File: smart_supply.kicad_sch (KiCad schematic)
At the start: 0 parts

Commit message: unify files
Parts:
- added C2: 0.1u, symbol Device:C
- added I1: ISIN, Package_SO:SOIC-20W_7.5x12.8mm_P1.27mm, symbol Simulation_SPICE:ISIN
- added R1: 50, symbol Device:R
- added R3, R4, R7, R8: 10k, symbol Device:R
- added R5: 220, symbol Device:R
- added R6: 10, symbol Device:R
- added TR1: ZMCT103C, Transformer_THT:Transformer_Zeming_ZMCT103C, symbol Transformer:ZMCT103C
- added V1: 3.3, symbol Simulation_SPICE:VDC
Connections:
- new net: I1.1, R5.1, R6.1
- new net: I1.2, R5.2, R7.1, R8.2
- new net: R8.1, V1.1
- new net: C2.2, R6.2
- new net: R1.2, R3.1, R4.2, TR1.2
- new net +3.3V: R3.2
- new net 0: C2.1, R7.2, V1.2
- new net GND: R4.1
- new net c_sns: R1.1, TR1.1
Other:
- note added: ".tran 0 200m 50m 10u"

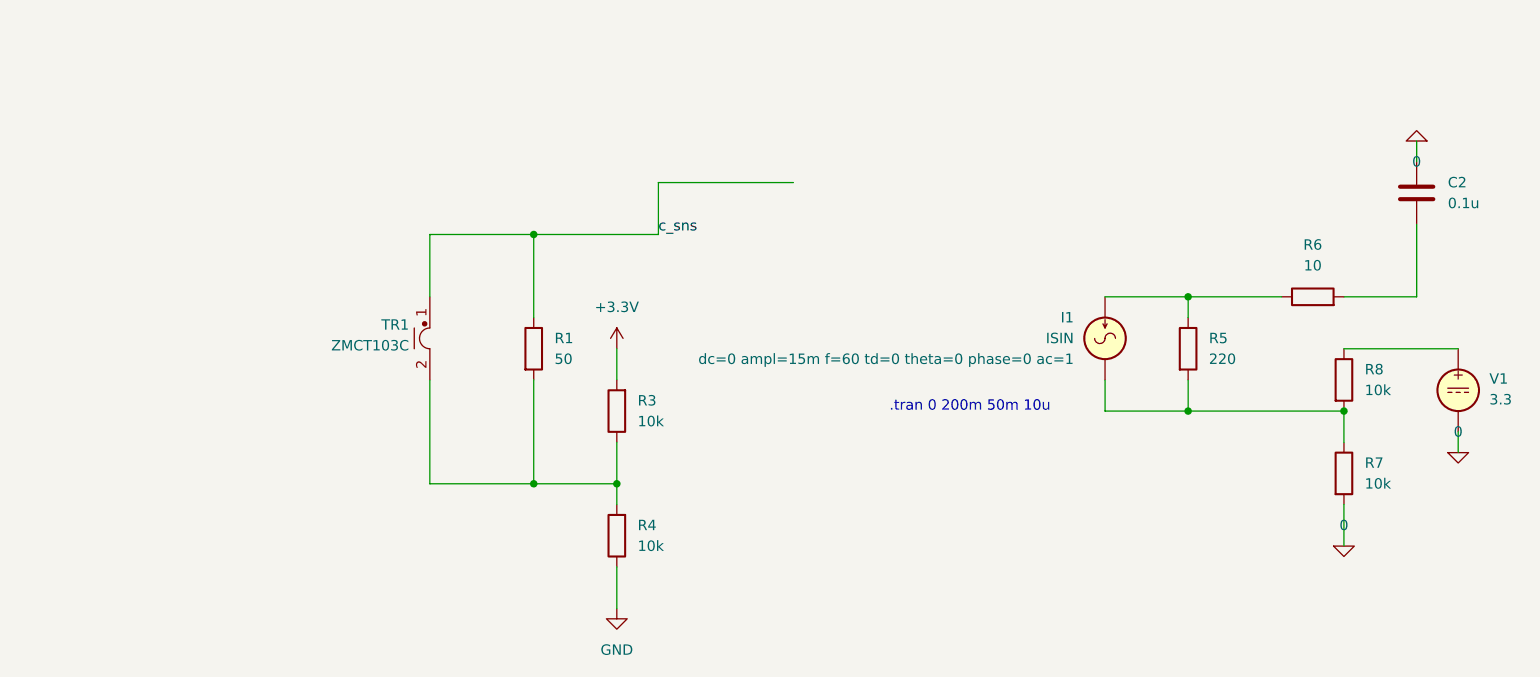
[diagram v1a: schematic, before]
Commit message: add current sense simulation
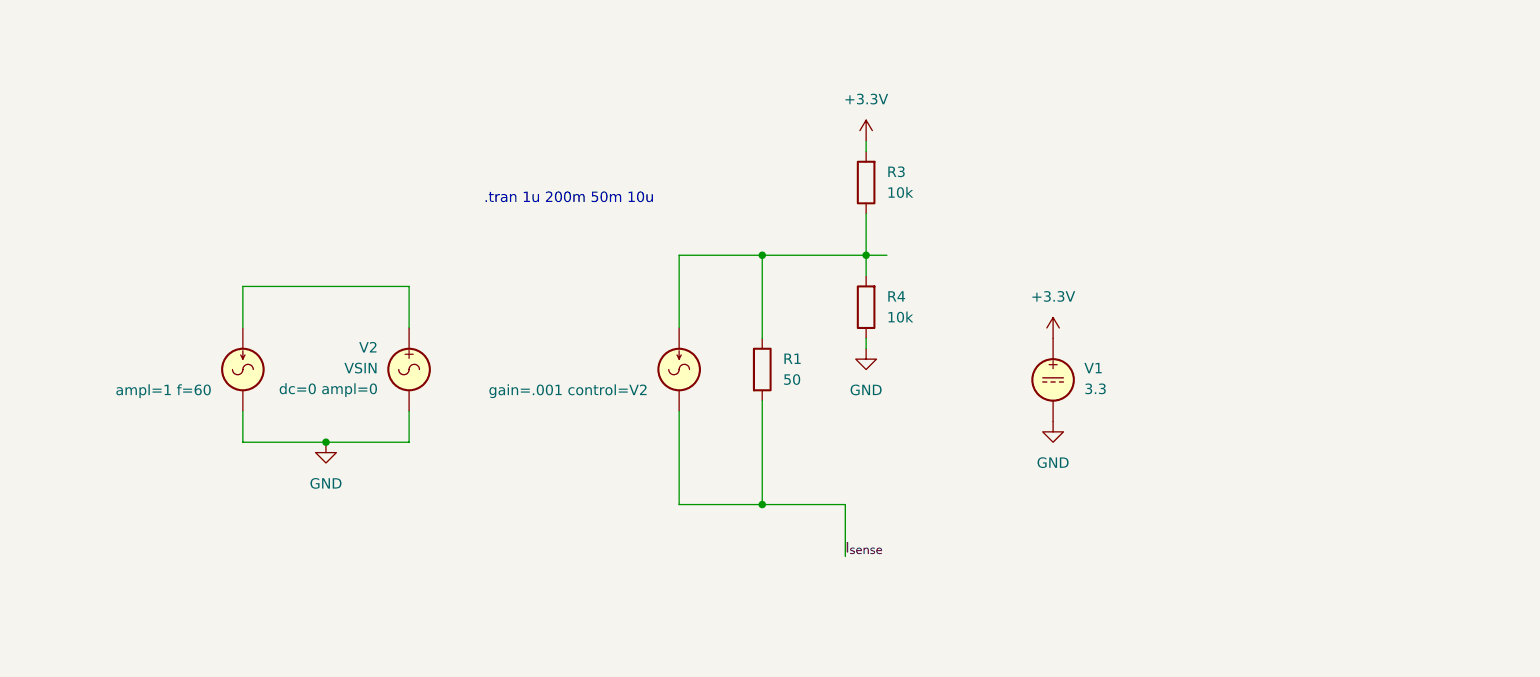
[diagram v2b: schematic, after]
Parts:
- removed C2: 0.1u, symbol Device:C
- removed I1: ISIN, Package_SO:SOIC-20W_7.5x12.8mm_P1.27mm, symbol Simulation_SPICE:ISIN
- removed R5: 220, symbol Device:R
- removed R6: 10, symbol Device:R
- removed R7, R8: 10k, symbol Device:R
- removed TR1: ZMCT103C, Transformer_THT:Transformer_Zeming_ZMCT103C, symbol Transformer:ZMCT103C
- added I2, I3: ISIN, Package_QFP:TQFP-44_10x10mm_P0.8mm, symbol Simulation_SPICE:ISIN
- added V2: VSIN, Package_QFP:TQFP-44_10x10mm_P0.8mm, symbol Simulation_SPICE:VSIN
- V1: footprint (none) -> Package_QFP:TQFP-44_10x10mm_P0.8mm
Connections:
- net 0 is gone; now on net GND: V1.2
- net c_sns is gone; now on an unnamed net: R1.1
- net +3.3V: now also V1.1
- net GND: now also I3.2, V2.2
- net at R3.1, R4.2: now also I2.1; no longer R1.2
- new net: I3.1, V2.1
- new net I_{sense}: I2.2, R1.2
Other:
- note added: ".tran 1u 200m 50m 10u"
- note removed: ".tran 0 200m 50m 10u"
- moved on the sheet: R1

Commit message: fix sheet hierarchy
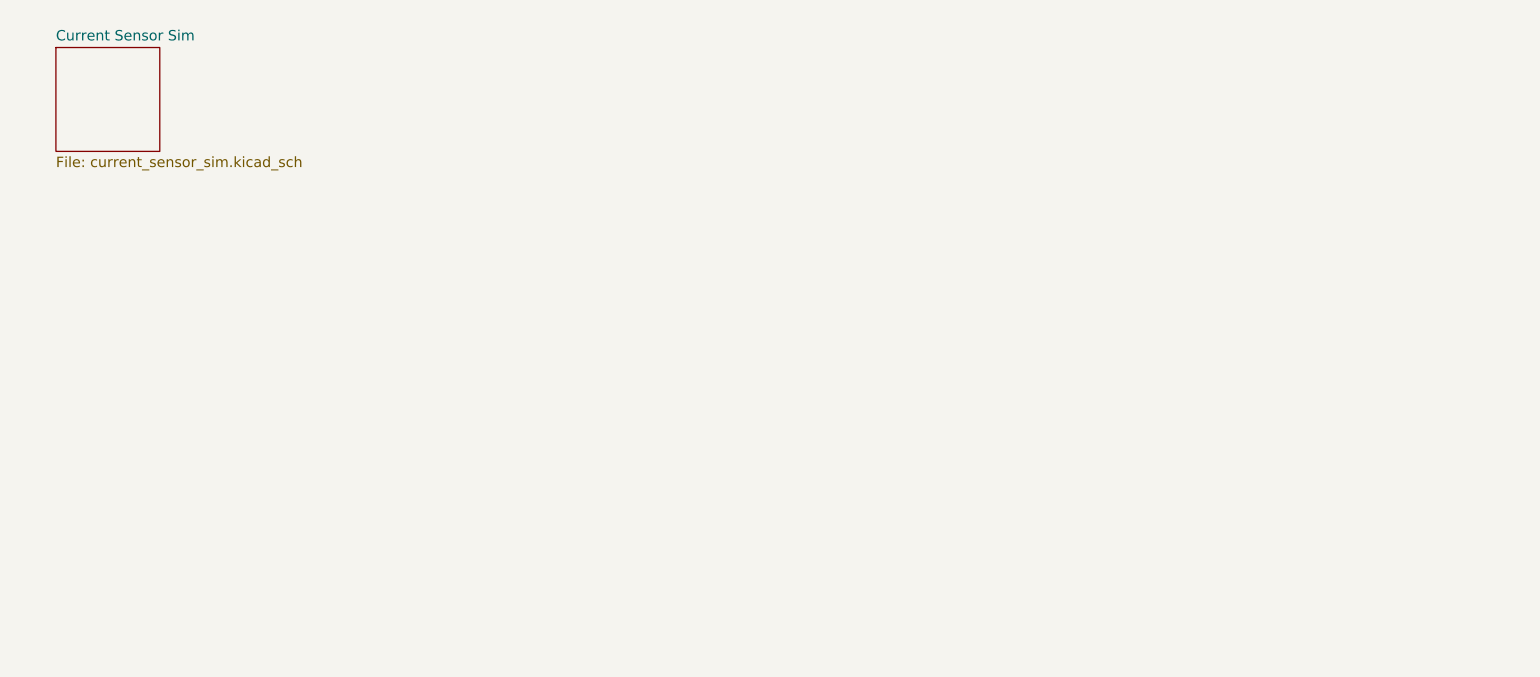
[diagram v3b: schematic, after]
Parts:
- removed I2, I3: ISIN, Package_QFP:TQFP-44_10x10mm_P0.8mm, symbol Simulation_SPICE:ISIN
- removed R1: 50, symbol Device:R
- removed R3, R4: 10k, symbol Device:R
- removed V1: 3.3, Package_QFP:TQFP-44_10x10mm_P0.8mm, symbol Simulation_SPICE:VDC
- removed V2: VSIN, Package_QFP:TQFP-44_10x10mm_P0.8mm, symbol Simulation_SPICE:VSIN
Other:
- added sheet Current Sensor Sim (current_sensor_sim.kicad_sch)
- note removed: ".tran 1u 200m 50m 10u"

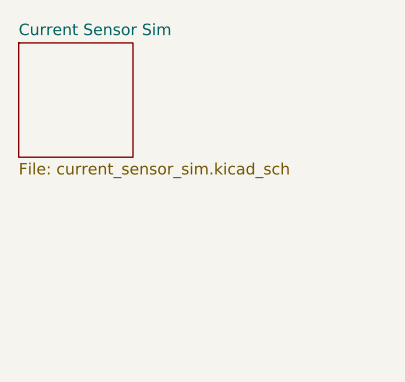
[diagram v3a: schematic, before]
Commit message: add mcu base
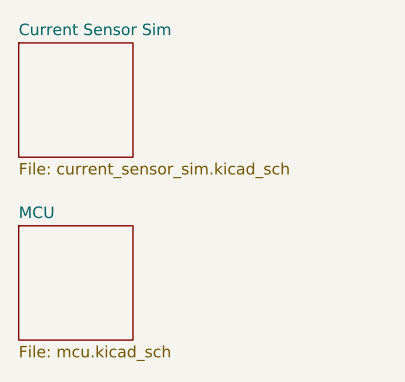
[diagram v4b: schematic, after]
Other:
- added sheet MCU (mcu.kicad_sch)
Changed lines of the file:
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@@
+		)
+	)
+	(sheet
+		(at 22.86 41.91)
+		(size 12.7 12.7)
+		(exclude_from_sim yes)
+		(in_bom yes)
+		(on_board yes)
+		(dnp no)
+		(fields_autoplaced yes)
+		(stroke
+			(width 0.1524)
+			(type solid)
+		)
+		(fill
+			(color 0 0 0 0)
+		)
+		(property "Sheetname" "MCU"
+			(at 22.86 41.1984 0)
+			(show_name no)
+			(do_not_autoplace no)
+			(effects
+				(font
+					(size 1.27 1.27)
+				)
+				(justify left bottom)
+			)
+		)
+		(property "Sheetfile" "mcu.kicad_sch"
+			(at 22.86 55.1946 0)
+			(show_name no)
+			(do_not_autoplace no)
+			(effects
+				(font
+					(size 1.27 1.27)
+				)
+				(justify left top)
+			)
+		)
+		(instances
+			(project "smart_supply"
+				(path "/487ef637-7a03-4925-80c1-798e0c6f0bbd"
+					(page "3")
+				)
+			)
 		)
 	)

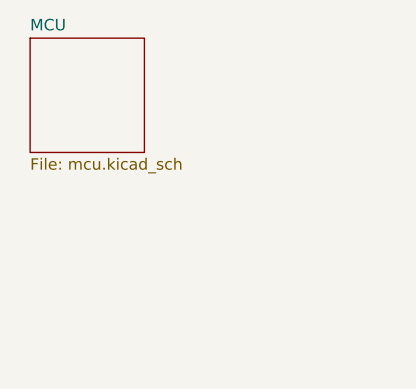
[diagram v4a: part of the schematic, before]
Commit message: Set buck passives, ADE intro
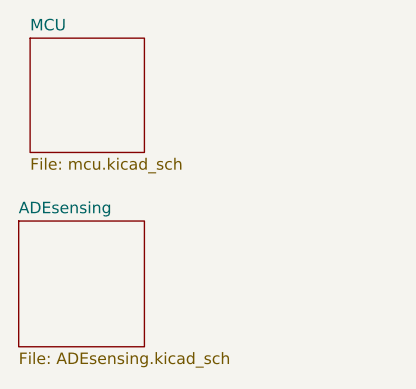
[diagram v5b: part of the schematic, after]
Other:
- added sheet ADEsensing (ADEsensing.kicad_sch)
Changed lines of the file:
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@@
 	(paper "A4")
+	(sheet
+		(at 21.59 62.23)
+		(size 13.97 13.97)
+		(exclude_from_sim no)
+		(in_bom yes)
+		(on_board yes)
+		(dnp no)
+		(fields_autoplaced yes)
+		(stroke
+			(width 0.1524)
+			(type solid)
+		)
+		(fill
+			(color 0 0 0 0)
+		)
+		(property "Sheetname" "ADEsensing"
+			(at 21.59 61.5184 0)
+			(show_name no)
+			(do_not_autoplace no)
+			(effects
+				(font
+					(size 1.27 1.27)
+				)
+				(justify left bottom)
+			)
+		)
+		(property "Sheetfile" "ADEsensing.kicad_sch"
+			(at 21.59 76.7846 0)
+			(show_name no)
+			(do_not_autoplace no)
+			(effects
+				(font
+					(size 1.27 1.27)
+				)
+				(justify left top)
+			)
+		)
+		(instances
+			(project "smart_supply"
+				(path "/487ef637-7a03-4925-80c1-798e0c6f0bbd"
+					(page "4")
+				)
+			)
+		)
+	)
 	(sheet
 		(at 22.86 21.59)

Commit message: ade7953 breakout board
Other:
- sheet ADEsensing renamed ADE Module
- added sheet Rectifier Simulation (rectifier_sim.kicad_sch)
- note added: "Layout"
- note added: "Simulation"
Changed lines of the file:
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@@
 	(generator_version "10.0")
 	(paper "A4")
-	(sheet
-		(at 21.59 62.23)
-		(size 13.97 13.97)
-		(exclude_from_sim no)
-		(in_bom yes)
-		(on_board yes)
-		(dnp no)
-		(fields_autoplaced yes)
-		(stroke
-			(width 0.1524)
-			(type solid)
-		)
-		(fill
-			(color 0 0 0 0)
-		)
-		(property "Sheetname" "ADEsensing"
-			(at 21.59 61.5184 0)
-			(show_name no)
-			(do_not_autoplace no)
-			(effects
-				(font
-					(size 1.27 1.27)
-				)
-				(justify left bottom)
-			)
-		)
-		(property "Sheetfile" "ADEsensing.kicad_sch"
-			(at 21.59 76.7846 0)
-			(show_name no)
-			(do_not_autoplace no)
-			(effects
-				(font
-					(size 1.27 1.27)
-				)
-				(justify left top)
-			)
-		)
-		(instances
-			(project "smart_supply"
-				(path "/487ef637-7a03-4925-80c1-798e0c6f0bbd"
-					(page "4")
-				)
-			)
-		)
-	)
-	(sheet
-		(at 22.86 21.59)
-		(size 12.7 12.7)
-		(exclude_from_sim no)
-		(in_bom no)
-		(on_board no)
-		(dnp no)
-		(fields_autoplaced yes)
-		(stroke
-			(width 0.1524)
-			(type solid)
-		)
-		(fill
-			(color 0 0 0 0)
-		)
-		(property "Sheetname" "Current Sensor Sim"
-			(at 22.86 20.8784 0)
-			(show_name no)
-			(do_not_autoplace no)
-			(effects
-				(font
-					(size 1.27 1.27)
-				)
-				(justify left bottom)
-			)
-		)
-		(property "Sheetfile" "current_sensor_sim.kicad_sch"
-			(at 22.86 34.8746 0)
-			(show_name no)
-			(do_not_autoplace no)
-			(effects
-				(font
-					(size 1.27 1.27)
-				)
-				(justify left top)
-			)
-		)
-		(instances
-			(project "smart_supply"
-				(path "/487ef637-7a03-4925-80c1-798e0c6f0bbd"
-					(page "2")
-				)
-			)
-		)
-	)
-	(sheet
-		(at 22.86 41.91)
+	(rectangle
+		(start 92.71 17.78)
+		(end 166.37 68.58)
+		(stroke
+			(width 0)
+			(type default)
+		)
+		(fill
+			(type none)
+		)
+	)
+	(rectangle
+		(start 19.05 17.78)
+		(end 92.71 68.58)
+		(stroke
+			(width 0)
+			(type default)
+		)
+		(fill
+			(type none)
+		)
+	)
+	(text "Simulation"
+		(exclude_from_sim no)
+		(at 107.442 65.278 0)
+		(effects
+			(font
+				(size 3.2512 3.2512)
+				(thickness 0.6502)
+				(bold yes)
+				(color 255 153 0 1)
+			)
+		)
+	)
+	(text "Layout"
+		(exclude_from_sim no)
+		(at 27.94 65.278 0)
+		(effects
+			(font
+				(size 3.2512 3.2512)
+				(thickness 0.6502)
+				(bold yes)
+				(color 0 0 255 1)
+			)
+		)
+	)
+	(sheet
+		(at 21.59 41.91)
 		(size 12.7 12.7)
 		(exclude_from_sim yes)
@@
 			(color 0 0 0 0)
 		)
+		(property "Sheetname" "ADE Module"
+			(at 21.59 41.1984 0)
+			(show_name no)
+			(do_not_autoplace no)
+			(effects
+				(font
+					(size 1.27 1.27)
+				)
+				(justify left bottom)
+			)
+		)
+		(property "Sheetfile" "ADEsensing.kicad_sch"
+			(at 21.59 55.1946 0)
+			(show_name no)
+			(do_not_autoplace no)
+			(effects
+				(font
+					(size 1.27 1.27)
+				)
+				(justify left top)
+			)
+		)
+		(instances
+			(project "smart_supply"
+				(path "/487ef637-7a03-4925-80c1-798e0c6f0bbd"
+					(page "5")
+				)
+			)
+		)
+	)
+	(sheet
+		(at 109.22 44.45)
+		(size 13.97 12.7)
+		(exclude_from_sim no)
+		(in_bom no)
+		(on_board no)
+		(dnp no)
+		(fields_autoplaced yes)
+		(stroke
+			(width 0.1524)
+			(type solid)
+		)
+		(fill
+			(color 0 0 0 0)
+		)
+		(property "Sheetname" "Current Sensor Sim"
+			(at 109.22 43.7384 0)
+			(show_name no)
+			(do_not_autoplace no)
+			(effects
+				(font
+					(size 1.27 1.27)
+				)
+				(justify left bottom)
+			)
+		)
+		(property "Sheetfile" "current_sensor_sim.kicad_sch"
+			(at 109.22 57.7346 0)
+			(show_name no)
+			(do_not_autoplace no)
+			(effects
+				(font
+					(size 1.27 1.27)
+				)
+				(justify left top)
+			)
+		)
+		(instances
+			(project "smart_supply"
+				(path "/487ef637-7a03-4925-80c1-798e0c6f0bbd"
+					(page "2")
+				)
+			)
+		)
+	)
+	(sheet
+		(at 109.22 24.13)
+		(size 13.97 13.97)
+		(exclude_from_sim no)
+		(in_bom no)
+		(on_board no)
+		(dnp no)
+		(fields_autoplaced yes)
+		(stroke
+			(width 0.1524)
+			(type solid)
+		)
+		(fill
+			(color 0 0 0 0)
+		)
+		(property "Sheetname" "Rectifier Simulation"
+			(at 109.22 23.4184 0)
+			(show_name no)
+			(do_not_autoplace no)
+			(effects
+				(font
+					(size 1.27 1.27)
+				)
+				(justify left bottom)
+			)
+		)
+		(property "Sheetfile" "rectifier_sim.kicad_sch"
+			(at 109.22 38.6846 0)
+			(show_name no)
+			(do_not_autoplace no)
+			(effects
+				(font
+					(size 1.27 1.27)
+				)
+				(justify left top)
+			)
+		)
+		(instances
+			(project "smart_supply"
+				(path "/487ef637-7a03-4925-80c1-798e0c6f0bbd"
+					(page "3")
+				)
+			)
+		)
+	)
+	(sheet
+		(at 21.59 21.59)
+		(size 12.7 12.7)
+		(exclude_from_sim yes)
+		(in_bom no)
+		(on_board no)
+		(dnp no)
+		(fields_autoplaced yes)
+		(stroke
+			(width 0.1524)
+			(type solid)
+		)
+		(fill
+			(color 0 0 0 0)
+		)
 		(property "Sheetname" "MCU"
-			(at 22.86 41.1984 0)
+			(at 21.59 20.8784 0)
 			(show_name no)
 			(do_not_autoplace no)
@@
 		)
 		(property "Sheetfile" "mcu.kicad_sch"
-			(at 22.86 55.1946 0)
-			(show_name no)
-			(do_not_autoplace no)
-			(effects
-				(font
-					(size 1.27 1.27)
-				)
-				(justify left top)
-			)
-		)
-		(instances
-			(project "smart_supply"
-				(path "/487ef637-7a03-4925-80c1-798e0c6f0bbd"
-					(page "3")
-				)
-			)
+			(at 21.59 34.8746 0)
+			(show_name no)
+			(do_not_autoplace no)
+			(effects
+				(font
+					(size 1.27 1.27)
+				)
+				(justify left top)
+			)
+		)
+		(instances
+			(project "smart_supply"
+				(path "/487ef637-7a03-4925-80c1-798e0c6f0bbd"
+					(page "4")
+				)
+			)

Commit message: TRANSFORMERS AND ADE
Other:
- added sheet ADE_final (ADE_final.kicad_sch)
- added sheet POWER LINES (POWER_LINES.kicad_sch)
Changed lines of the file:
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@@
+	)
+	(sheet
+		(at 49.53 41.91)
+		(size 12.7 12.7)
+		(exclude_from_sim yes)
+		(in_bom no)
+		(on_board no)
+		(dnp no)
+		(fields_autoplaced yes)
+		(stroke
+			(width 0.1524)
+			(type solid)
+		)
+		(fill
+			(color 0 0 0 0)
+		)
+		(property "Sheetname" "POWER LINES"
+			(at 49.53 41.1984 0)
+			(show_name no)
+			(do_not_autoplace no)
+			(effects
+				(font
+					(size 1.27 1.27)
+				)
+				(justify left bottom)
+			)
+		)
+		(property "Sheetfile" "POWER_LINES.kicad_sch"
+			(at 49.53 55.1946 0)
+			(show_name no)
+			(do_not_autoplace no)
+			(effects
+				(font
+					(size 1.27 1.27)
+				)
+				(justify left top)
+			)
+		)
+		(instances
+			(project "smart_supply"
+				(path "/487ef637-7a03-4925-80c1-798e0c6f0bbd"
+					(page "7")
+				)
+			)
+		)
 	)
 	(sheet
@@
 				)
 			)
+		)
+	)
+	(sheet
+		(at 49.53 21.59)
+		(size 12.7 12.7)
+		(exclude_from_sim yes)
+		(in_bom no)
+		(on_board no)
+		(dnp no)
+		(fields_autoplaced yes)
+		(stroke
+			(width 0.1524)
+			(type solid)
+		)
+		(fill
+			(color 0 0 0 0)
+		)
+		(property "Sheetname" "ADE_final"
+			(at 49.53 20.8784 0)
+			(show_name no)
+			(do_not_autoplace no)
+			(effects
+				(font
+					(size 1.27 1.27)
+				)
+				(justify left bottom)
+			)
+		)
+		(property "Sheetfile" "ADE_final.kicad_sch"
+			(at 49.53 34.8746 0)
+			(show_name no)
+			(do_not_autoplace no)
+			(effects
+				(font
+					(size 1.27 1.27)
+				)
+				(justify left top)
+			)
+		)
+		(instances
+			(project "smart_supply"
+				(path "/487ef637-7a03-4925-80c1-798e0c6f0bbd"
+					(page "6")
+				)
+			)
